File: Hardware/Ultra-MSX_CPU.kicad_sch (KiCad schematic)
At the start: 24 parts, among them J11 Conn_02x05_Odd_Even, J15 Battery_2x_SR66_holder, U1 MPU_Z380, U5 BQ4802YPW, Y2 Crystal_AB38T-32.768KHZ

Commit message: Multiple redesigns of the IO-shield. Replaced FPGA with lower pin-count AT10K, since the higher pin-count one is now obsolete.
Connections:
- net +3V3 renamed +3.3V

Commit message: Added cooler and CPU-mount footprints, as well as Indication LEDs.
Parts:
- added R47, R48, R49, R50, R51, R52, R53, R54: R_RC0603FR-0710KL, LRJ:R_0603_1608Metric_roundcourt, symbol LRJ-parts:R_RC0603FR-0710KL
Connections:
- net +5V: now also R47.1, R48.1, R49.1, R50.1, R51.1, R52.1, R53.1, R54.1
- net D10: now also R49.2
- net D11: now also R50.2
- net D12: now also R51.2
- net D13: now also R52.2
- net D14: now also R53.2
- net D15: now also R54.2
- net D8: now also R47.2
- net D9: now also R48.2
- net CLK_VDP: no longer names the net of U1.25 (CLKI)
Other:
- note removed: "MSX-engine chips: ------------ PPI ---- v- 7400 (four 2-input NAND) v- 7430 (x2) (8-input NAND) v- 7432 (x3) (four 2-input OR) v- 74273 (x2) (eight D-type flip-flop with reset; positive-edge trigger) -74540 (Octal buffer/line driver; inverting) -74541 (x3) (8-bit Buffer/Line Driver) v- 74153 (x2) (two 4-input multiplexer) v- 8255 Logic: 7x2 NAND + 4 NAND (18 NAND) 4x3 OR (36 NAND) 8x2 Flip-flop (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"
- moved on the sheet: R16, R62, R63, R64, R65, R66, R67, R68, R69, R70, R71, R72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

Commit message: Started fixing many small issues.
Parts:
- added D5: LED_VLMB1310, LED_SMD:LED_0603_1608Metric, symbol LRJ-parts:LED_VLMB1310
- added Q1: DMN2058, Package_TO_SOT_SMD:SOT-23, symbol LRJ-parts:DMN2058
- added R60: R_ERJ-3EKF10R0V, Resistor_SMD:R_0603_1608Metric, symbol LRJ-parts:R_ERJ-3EKF10R0V
- virt_sym1: footprint LRJ:TestPoint_Bridge_Pitch1.5mm_Pad0.8mm -> (none)
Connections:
- net +3.3V: now also D5.2 (A)
- net +5VSB: now also virt_sym1.2; no longer virt_sym1.1
- net GND: now also Q1.3 (D)
- net HD+: now also D5.1 (K), Q1.2 (S)
- new net: Q1.1 (G), R60.2
- new net HDD_PWM: R60.1
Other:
- note added: "0"
- note added: "0000 ~ 3FFF"
- note added: "0000 ~ FFFF"
- note added: "00000000"
- note added: "00FFFFFF"
- note added: "1"
- note added: "16 KB"
- note added: "2"
- note added: "3-0"
- note added: "3-1"
- note added: "3-2"
- note added: "3-3"
- note added: "32 KB"
- note added: "3FFF = 16 KB; 4000 = 16 KB; 7FFF = 32 KB;"
- note added: "4/8/16 KB"
- note added: "4000 ~ 7FFF"
- note added: "4000 ~ FFFF"
- note added: "48 KB"
- note added: "64 KB"
- note added: "8 KB"
- note added: "8000 = 32 KB; BFFF = 48 KB;"
- note added: "8000 ~ 9FFF"
- note added: "8000 ~ BFFF"
- note added: "?"
- note added: "A000 ~ BFFF"
- note added: "ADDRESS"
- note added: "All Mem-CS within first 16Mbytes of Memory (5,33 MB per region??) Hypothesis: All MSX slots can fit into LMCS-region."
- note added: "C000 = 48 KB; FFFF = 64 KB"
- note added: "C000 ~ DFFF"
- note added: "C000 ~ FFFF"
- note added: "CART 1"
- note added: "CART 2"
- note added: "CONTENTS"
- note added: "Control signals"
- note added: "E000 ~ FFFF"
- note added: "Front panel"
- note added: "HDD LED switcher"
- note added: "LMCS"
- note added: "Lower"
- note added: "MCS0"
- note added: "MCS0 MCS1 MCS2 MCS3"
- note added: "MEM.MAPR"
- note added: "Main-ROM"
- note added: "Mid-Range"
- note added: "Omega alternate map:"
- note added: "Omega chip-select chain: [Z80]WR/IORQ/M1 ->[SPLD]RTC_CS ->[WD]RTC_CS_B ->[RTC]Alarm??"
- note added: "Omega slot map:"
- note added: "REGION"
- note added: "SIGNAL"
- note added: "SIZE"
- note added: "SLOT"
- note added: "SUB-ROM"
- note added: "T1"
- note added: "T2"
- note added: "T3"
- note added: "T3-0 T3-1 T3-2 T3-3"
- note added: "UMCS"
- note added: "USR-ROM"
- note added: "Upper"
- note added: "WAIT-STATE"
- note added: "Z380 Memory map 1:"
- note added: "Z380 Memory map 2:"
- note added: "[FREE]"
- note removed: "Chips integrated already into Z280: -------------- 256 byte Cache High performance 16-bit Z-BUS interface or 8-bit Z80-compatible bus interface MMU Four 16-bit counter/timers 4 DMA channels Full duplex UART Burst mode memory access Accelerated communication interface"
- note removed: "MEMORY MAPPING: ---------------- - have 512K available for direct addressing in combination with the standard FC/FD/FE/FF ports - make another port available(which can accept 8bit,16bit, 32bit or even larger page numbers..fed sequentially) for some sub-switching to a larger memory. - to unload the processor with moving/clearing/copying one can add something as simple as a microcontroller to move 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"
- note removed: "Reset-design: https://semiengineering.com/respecting-reset/"
- moved on the sheet: C24, C25, C26, R26, U1B, U1D, Y2

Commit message: Updated the readme, silenced multiple errors in Kicad regarding simulation-files.
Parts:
- removed virt_sym1: Virtual_symbol, symbol LRJ-parts:Virtual_symbol
- added trace2: pcb-trace, LRJ:NetTie-2_SMD_Pad0.2mm, symbol LRJ-parts:Trace_0.2mm
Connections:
- net +5VSB: now also trace2.2
- net at U1.42 (~{STNBY}): now also trace2.1

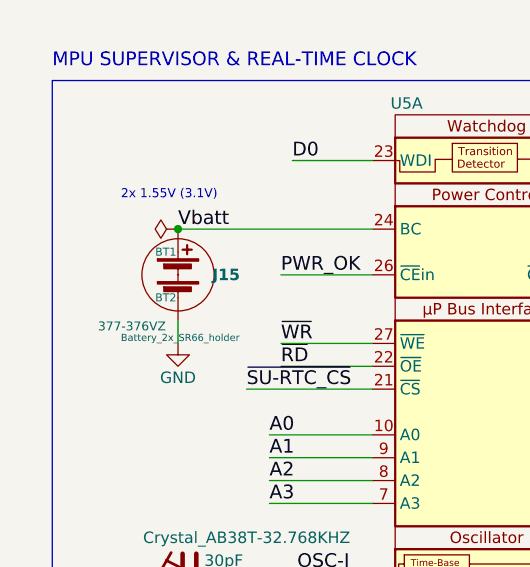
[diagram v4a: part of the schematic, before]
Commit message: Many tweaks and changes, such as a slight redesign of the VDP-baord.
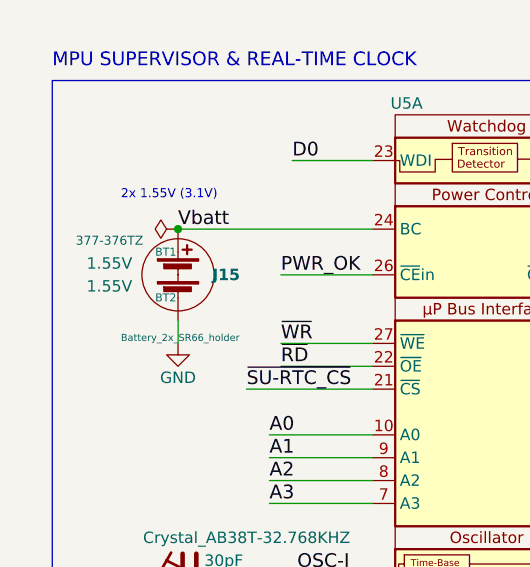
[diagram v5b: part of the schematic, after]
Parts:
- BT1, BT2: value Battery_377-376VZ_dummy -> Battery_377-376TZ_dummy; symbol LRJ-parts:Battery_377-376VZ_dummy -> LRJ-parts:Battery_377-376TZ_dummy; MPN 377-376VZ -> 377-376TZ; Status (none) -> Active
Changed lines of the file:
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@@
     )
   )
-  (symbol (lib_id "LRJ-parts:Battery_377-376VZ_dummy") (at 38.1 135.89 0) (unit 1)
+  (symbol (lib_id "LRJ-parts:Battery_377-376TZ_dummy") (at 38.1 135.89 0) (unit 1)
     (in_bom yes) (on_board yes) (dnp no)
     (property "Reference" "BT1" (at 35.56 133.35 0)
       (effects (font (size 0.889 0.889)) (justify left))
     )
-    (property "Value" "Battery_377-376VZ_dummy" (at 27.94 146.05 0)
+    (property "Value" "Battery_377-376TZ_dummy" (at 27.94 146.05 0)
       (effects (font (size 1.27 1.27)) (justify left) hide)
     )
@@
       (effects (font (size 1.27 1.27)) hide)
     )
-    (property "Datasheet" "https://data.energizer.com/pdfs/377-376Z.pdf" (at 38.1 134.366 90)
+    (property "Datasheet" "https://data.energizer.com/pdfs/377-376z.pdf" (at 38.1 134.366 90)
       (effects (font (size 1.27 1.27)) hide)
     )
@@
       (effects (font (size 1.524 1.524)) hide)
     )
-    (property "MPN" "377-376VZ" (at 29.21 141.605 0)
-      (effects (font (size 0.9906 0.9906)) (justify left))
+    (property "MPN" "377-376TZ" (at 30.48 132.08 0)
+      (effects (font (size 1 1)))
     )
-    (property "Voltage" "1.55V" (at 29.21 136.525 0)
-      (effects (font (size 0.9906 0.9906)) (justify left) hide)
+    (property "Voltage" "1.55V" (at 30.48 134.62 0)
+      (effects (font (size 1.27 1.27)))
     )
     (property "Sim.Enable" "0" (at 38.1 135.89 0)
+      (effects (font (size 1.27 1.27)) hide)
+    )
+    (property "Status" "Active" (at 55.88 138.43 0)
       (effects (font (size 1.27 1.27)) hide)
     )
@@
     )
   )
-  (symbol (lib_id "LRJ-parts:Battery_377-376VZ_dummy") (at 38.1 138.43 0) (unit 1)
+  (symbol (lib_id "LRJ-parts:Battery_377-376TZ_dummy") (at 38.1 138.43 0) (unit 1)
     (in_bom yes) (on_board yes) (dnp no)
     (property "Reference" "BT2" (at 35.56 138.43 0)
       (effects (font (size 0.889 0.889)) (justify left))
     )
-    (property "Value" "Battery_377-376VZ_dummy" (at 27.94 148.59 0)
+    (property "Value" "Battery_377-376TZ_dummy" (at 27.94 148.59 0)
       (effects (font (size 1.27 1.27)) (justify left) hide)
     )
@@
       (effects (font (size 1.27 1.27)) hide)
     )
-    (property "Datasheet" "https://data.energizer.com/pdfs/377-376Z.pdf" (at 38.1 136.906 90)
+    (property "Datasheet" "https://data.energizer.com/pdfs/377-376z.pdf" (at 38.1 136.906 90)
       (effects (font (size 1.27 1.27)) hide)
     )
@@
       (effects (font (size 1.524 1.524)) hide)
     )
-    (property "MPN" "377-376VZ" (at 41.0972 138.3284 0)
-      (effects (font (size 1.524 1.524)) (justify left) hide)
+    (property "MPN" "377-376TZ" (at 26.67 135.89 0)
+      (effects (font (size 1.524 1.524)) hide)
     )
-    (property "Voltage" "1.55V" (at 41.0972 139.6746 0)
-      (effects (font (size 1.524 1.524)) (justify left) hide)
+    (property "Voltage" "1.55V" (at 30.48 137.16 0)
+      (effects (font (size 1.27 1.27)))
     )
     (property "Sim.Enable" "0" (at 38.1 138.43 0)
       (effects (font (size 1.27 1.27)) hide)
     )
+    (property "Status" "Active" (at 55.88 140.97 0)
+      (effects (font (size 1.27 1.27)) hide)
+    )

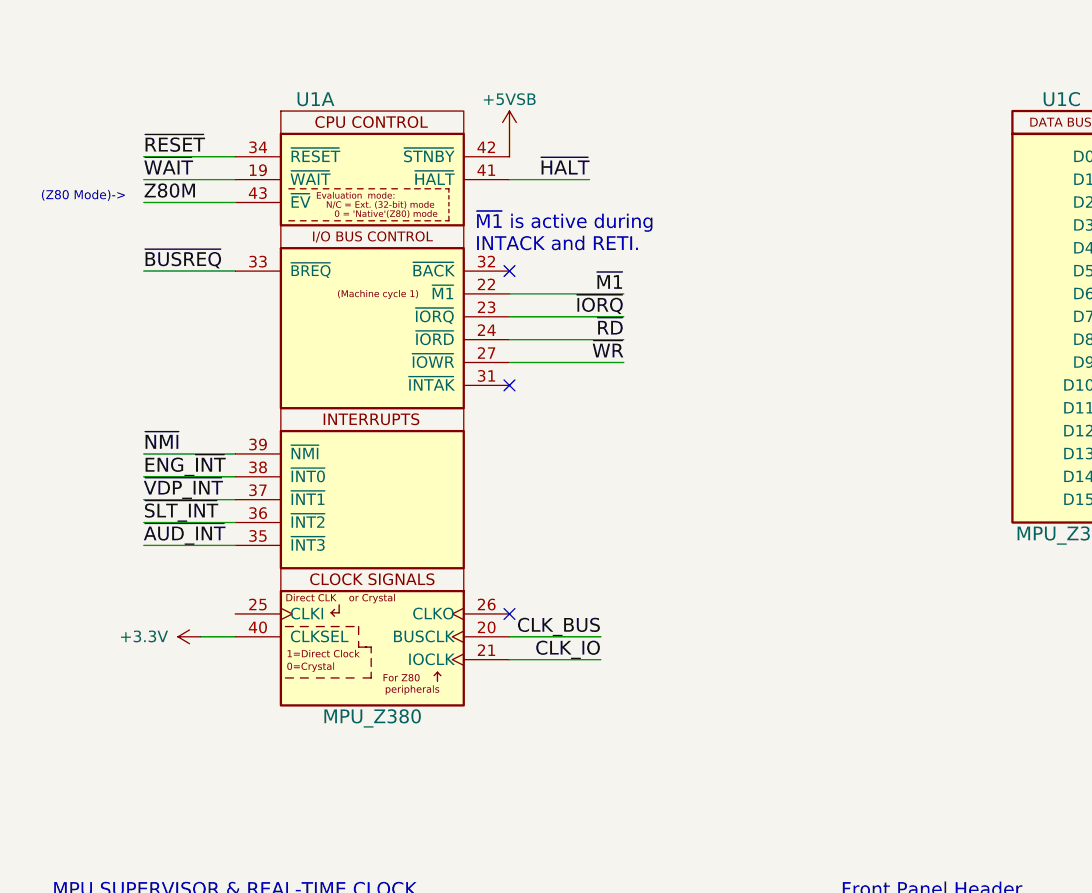
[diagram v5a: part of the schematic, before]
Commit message: Returned to Simm-72 memory module to simplify design, returned to AT40K40 with 254 io, FPGA.
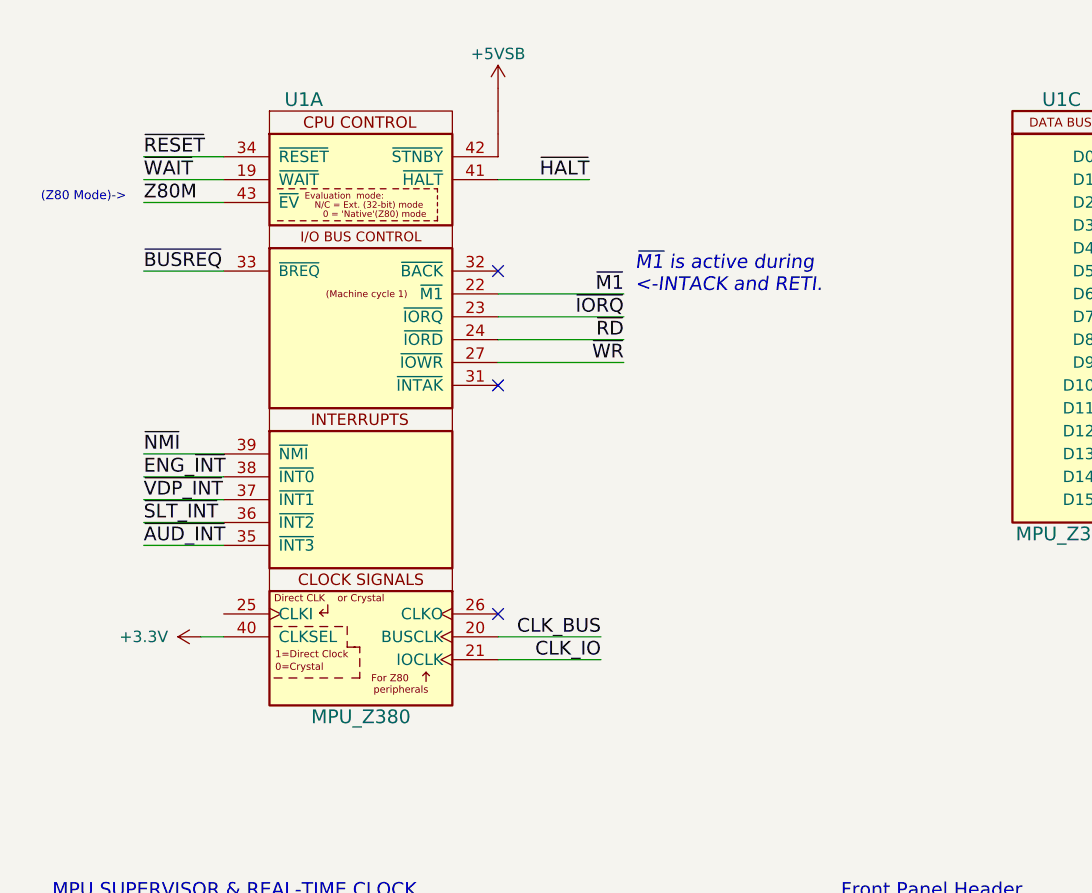
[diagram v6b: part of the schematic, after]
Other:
- note added: "~{M1} is active during <-INTACK and RETI."
- note removed: "~{M1} is active during INTACK and RETI."
- moved on the sheet: U1A
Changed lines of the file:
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@@
   (junction (at 210.82 59.69) (diameter 0) (color 0 0 0 0)
   )
-  (no_connect (at 74.93 43.18))
-  (no_connect (at 74.93 81.28))
+  (no_connect (at 73.66 43.18))
+  (no_connect (at 73.66 81.28))
   (no_connect (at 147.32 120.65))
-  (no_connect (at 74.93 55.88))
+  (no_connect (at 73.66 55.88))
   (bus_entry (at 387.35 25.4) (size 2.54 2.54)
     (stroke (width 0) (type default))
@@
     (stroke (width 0) (type default))
   )
-  (wire (pts (xy 74.93 50.8) (xy 87.63 50.8))
+  (wire (pts (xy 73.66 50.8) (xy 87.63 50.8))
     (stroke (width 0) (type default))
   )
@@
     (stroke (width 0) (type default))
   )
-  (wire (pts (xy 74.93 83.82) (xy 85.09 83.82))
+  (wire (pts (xy 73.66 83.82) (xy 85.09 83.82))
     (stroke (width 0) (type default))
   )
@@
     (stroke (width 0) (type default))
   )
-  (wire (pts (xy 44.45 73.66) (xy 34.29 73.66))
+  (wire (pts (xy 43.18 73.66) (xy 34.29 73.66))
     (stroke (width 0) (type default))
   )
@@
     (stroke (width 0) (type default))
   )
-  (wire (pts (xy 74.93 86.36) (xy 85.09 86.36))
+  (wire (pts (xy 73.66 86.36) (xy 85.09 86.36))
     (stroke (width 0) (type default))
   )
@@
     (stroke (width 0) (type default))
   )
-  (wire (pts (xy 40.64 83.82) (xy 44.45 83.82))
+  (wire (pts (xy 40.64 83.82) (xy 43.18 83.82))
     (stroke (width 0) (type default))
   )
@@
     (stroke (width 0) (type default))
   )
-  (wire (pts (xy 83.82 33.02) (xy 74.93 33.02))
+  (wire (pts (xy 83.82 33.02) (xy 73.66 33.02))
     (stroke (width 0) (type default))
   )
@@
     (stroke (width 0) (type default))
   )
-  (wire (pts (xy 74.93 48.26) (xy 87.63 48.26))
+  (wire (pts (xy 73.66 48.26) (xy 87.63 48.26))
     (stroke (width 0) (type default))
   )
-  (wire (pts (xy 44.45 68.58) (xy 34.29 68.58))
+  (wire (pts (xy 43.18 68.58) (xy 34.29 68.58))
     (stroke (width 0) (type default))
   )
@@
     (stroke (width 0) (type default))
   )
-  (wire (pts (xy 44.45 71.12) (xy 34.29 71.12))
+  (wire (pts (xy 43.18 71.12) (xy 34.29 71.12))
     (stroke (width 0) (type default))
   )
@@
     (stroke (width 0) (type default))
   )
-  (wire (pts (xy 34.29 33.02) (xy 44.45 33.02))
+  (wire (pts (xy 34.29 33.02) (xy 43.18 33.02))
     (stroke (width 0) (type default))
   )
@@
     (stroke (width 0) (type default))
   )
-  (wire (pts (xy 87.63 45.72) (xy 74.93 45.72))
+  (wire (pts (xy 87.63 45.72) (xy 73.66 45.72))
     (stroke (width 0) (type default))
   )
@@
     (stroke (width 0) (type default))
   )
-  (wire (pts (xy 34.29 35.56) (xy 44.45 35.56))
+  (wire (pts (xy 34.29 35.56) (xy 43.18 35.56))
     (stroke (width 0) (type default))
   )
@@
     (stroke (width 0) (type default))
   )
-  (wire (pts (xy 74.93 53.34) (xy 87.63 53.34))
+  (wire (pts (xy 73.66 53.34) (xy 87.63 53.34))
     (stroke (width 0) (type default))
   )
@@
     (stroke (width 0) (type default))
   )
-  (wire (pts (xy 34.29 66.04) (xy 44.45 66.04))
+  (wire (pts (xy 34.29 66.04) (xy 43.18 66.04))
     (stroke (width 0) (type default))
   )
@@
     (stroke (width 0) (type default))
   )
-  (wire (pts (xy 44.45 30.48) (xy 34.29 30.48))
+  (wire (pts (xy 43.18 30.48) (xy 34.29 30.48))
     (stroke (width 0) (type default))
   )
@@
     (stroke (width 0) (type default))
   )
-  (wire (pts (xy 44.45 43.18) (xy 34.29 43.18))
+  (wire (pts (xy 43.18 43.18) (xy 34.29 43.18))
     (stroke (width 0) (type default))
   )
@@
     (stroke (width 0) (type default))
   )
-  (wire (pts (xy 44.45 63.5) (xy 34.29 63.5))
+  (wire (pts (xy 43.18 63.5) (xy 34.29 63.5))
     (stroke (width 0) (type default))
   )
@@
     (effects (font (size 1.27 1.27)) (justify left bottom))
   )
-  (text "~{M1} is active during \nINTACK and RETI." (at 71.12 41.275 0)
-    (effects (font (size 1.524 1.524)) (justify left bottom))
+  (text "~{M1} is active during \n<-INTACK and RETI." (at 88.9 45.72 0)
+    (effects (font (size 1.524 1.524) italic) (justify left bottom))
   )
   (text "SIZE" (at 486.41 31.75 0)
@@
     )
   )
-  (symbol (lib_name "MPU_Z380_2") (lib_id "Ultra-MSX:MPU_Z380") (at 59.69 58.42 0) (unit 1)
+  (symbol (lib_name "MPU_Z380_2") (lib_id "Ultra-MSX:MPU_Z380") (at 58.42 58.42 0) (unit 1)
     (in_bom yes) (on_board yes) (dnp no)
-    (property "Reference" "U1" (at 53.34 24.13 0)
+    (property "Reference" "U1" (at 52.07 24.13 0)
       (effects (font (size 1.524 1.524)))
     )
-    (property "Value" "MPU_Z380" (at 59.69 92.71 0)
+    (property "Value" "MPU_Z380" (at 58.42 92.71 0)
       (effects (font (size 1.524 1.524)))
     )
-    (property "Footprint" "Package_QFP:PQFP-100_14x20mm_P0.65mm" (at 115.57 53.34 0)
+    (property "Footprint" "Package_QFP:PQFP-100_14x20mm_P0.65mm" (at 114.3 53.34 0)
       (effects (font (size 1.524 1.524)) hide)
     )
-    (property "Datasheet" "https://www.mouser.se/datasheet/2/240/z380-2584705.pdf" (at 57.15 25.4 0)
+    (property "Datasheet" "https://www.mouser.se/datasheet/2/240/z380-2584705.pdf" (at 55.88 25.4 0)
       (effects (font (size 1.524 1.524)) hide)
     )
-    (property "Manufacturer" "Zilog Inc." (at 95.25 40.64 0)
+    (property "Manufacturer" "Zilog Inc." (at 93.98 40.64 0)
       (effects (font (size 1.524 1.524)) hide)
     )
-    (property "MPN" "Z80380" (at 92.71 43.18 0)
+    (property "MPN" "Z80380" (at 91.44 43.18 0)
       (effects (font (size 1.524 1.524)) hide)
     )
-    (property "Operating temperature" "-40 to +100 C" (at 99.06 46.99 0)
+    (property "Operating temperature" "-40 to +100 C" (at 97.79 46.99 0)
       (effects (font (size 1.524 1.524)) hide)
     )
-    (property "Frequency" "6-25 MHz" (at 95.885 50.165 0)
+    (property "Frequency" "6-25 MHz" (at 94.615 50.165 0)
       (effects (font (size 1.524 1.524)) hide)
     )
-    (property "Status" "OBSOLETE" (at 95.25 55.88 0)
+    (property "Status" "OBSOLETE" (at 93.98 55.88 0)
       (effects (font (size 1.524 1.524)) hide)
     )
-    (property "Sim.Enable" "0" (at 59.69 58.42 0)
+    (property "Sim.Enable" "0" (at 58.42 58.42 0)
       (effects (font (size 1.27 1.27)) hide)
     )
@@
     )
   )
-  (symbol (lib_id "LRJ-parts:Trace_0.2mm") (at 74.93 30.48 0) (unit 1)
+  (symbol (lib_id "LRJ-parts:Trace_0.2mm") (at 73.66 25.4 0) (unit 1)
     (in_bom no) (on_board yes) (dnp no) (fields_autoplaced)
-    (property "Reference" "trace2" (at 80.01 27.94 0)
+    (property "Reference" "trace2" (at 78.74 22.86 0)
       (effects (font (size 1.27 1.27)) hide)
     )
-    (property "Value" "pcb-trace" (at 82.55 30.48 0)
+    (property "Value" "pcb-trace" (at 81.28 25.4 0)
       (effects (font (size 1.27 1.27)) hide)
     )
-    (property "Footprint" "LRJ:NetTie-2_SMD_Pad0.2mm" (at 74.93 33.02 0)
+    (property "Footprint" "LRJ:NetTie-2_SMD_Pad0.2mm" (at 73.66 27.94 0)
       (effects (font (size 1.27 1.27)) hide)
     )
-    (property "Datasheet" "" (at 77.47 27.94 0)
+    (property "Datasheet" "" (at 76.2 22.86 0)
       (effects (font (size 1.27 1.27)) hide)
     )
-    (property "Sim.Enable" "0" (at 74.93 30.48 0)
+    (property "Sim.Enable" "0" (at 73.66 25.4 0)
       (effects (font (size 1.27 1.27)) hide)
     )
@@
     )
   )
-  (symbol (lib_id "LRJ-parts:+5VSB") (at 74.93 27.94 0) (unit 1)
+  (symbol (lib_id "LRJ-parts:+5VSB") (at 73.66 22.86 0) (unit 1)
     (in_bom no) (on_board yes) (dnp no)
-    (property "Reference" "#PWR034" (at 74.93 31.75 0)
+    (property "Reference" "#PWR034" (at 73.66 26.67 0)
       (effects (font (size 1.27 1.27)) hide)
     )
-    (property "Value" "+5VSB" (at 74.93 24.13 0)
+    (property "Value" "+5VSB" (at 73.66 19.05 0)
       (effects (font (size 1.27 1.27)))
     )
-    (property "Footprint" "" (at 74.93 27.94 0)
+    (property "Footprint" "" (at 73.66 22.86 0)
       (effects (font (size 1.27 1.27)) hide)
     )
-    (property "Datasheet" "" (at 74.93 27.94 0)
+    (property "Datasheet" "" (at 73.66 22.86 0)
       (effects (font (size 1.27 1.27)) hide)
     )
-    (property "Description" "Standby-power, 10 mA max (ATX v.1.x) or  2A max (ATX v.2.2+)" (at 74.93 38.1 0)
+    (property "Description" "Standby-power, 10 mA max (ATX v.1.x) or  2A max (ATX v.2.2+)" (at 73.66 33.02 0)
       (effects (font (size 1.27 1.27)) hide)
     )
